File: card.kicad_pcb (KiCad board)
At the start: 2 copper layers, 38.6 x 52.3 mm, 83 parts, among them J1 Conn_01x20_Male, J2 HDMI_A, J3 Conn_01x20_Male, J4 USB_B_Micro, SW1 SW_DPST_x2, U1 SPX3819-1.8, U2 IMP811REUS-T, U3 SP6205EM5-L-3-3_TR, U4 MP1469GJ, U5 W25Q32JVSS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

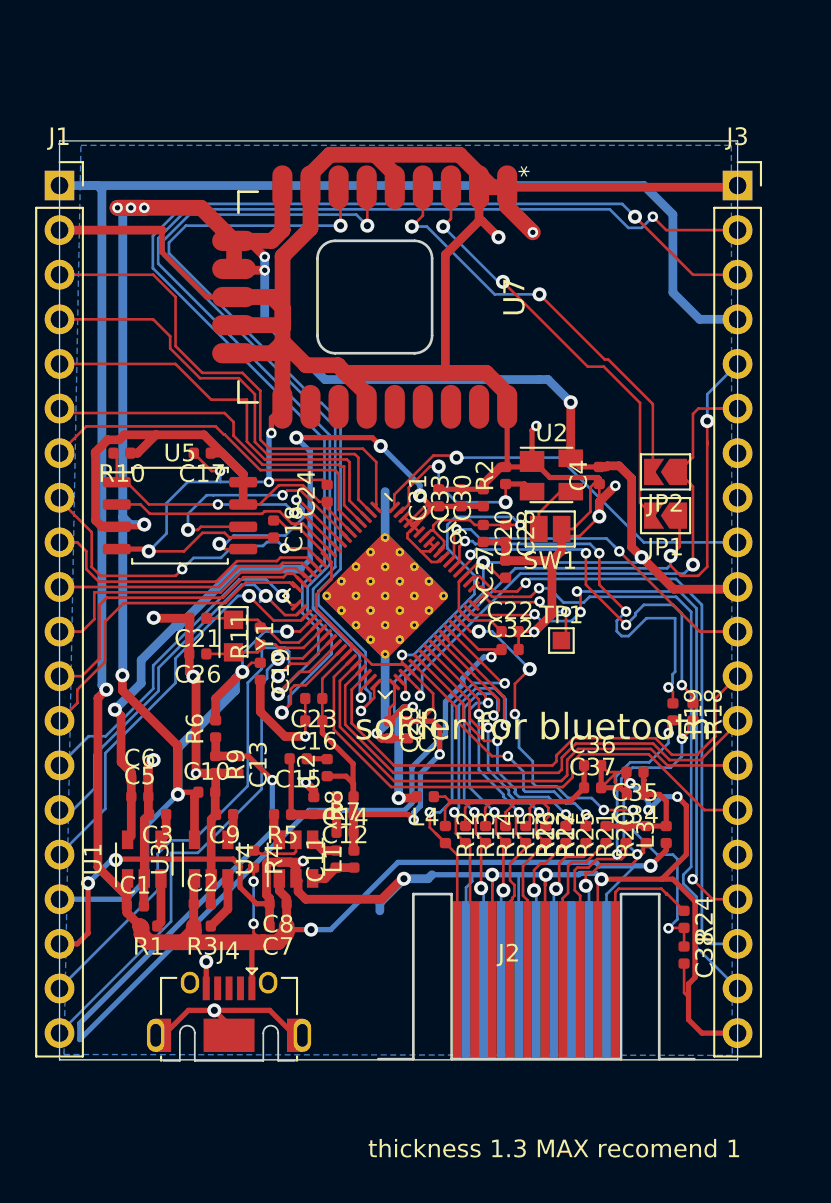
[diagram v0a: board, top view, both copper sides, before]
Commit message: finished routing, and started neatnening up some of the ugly traces and silk screen
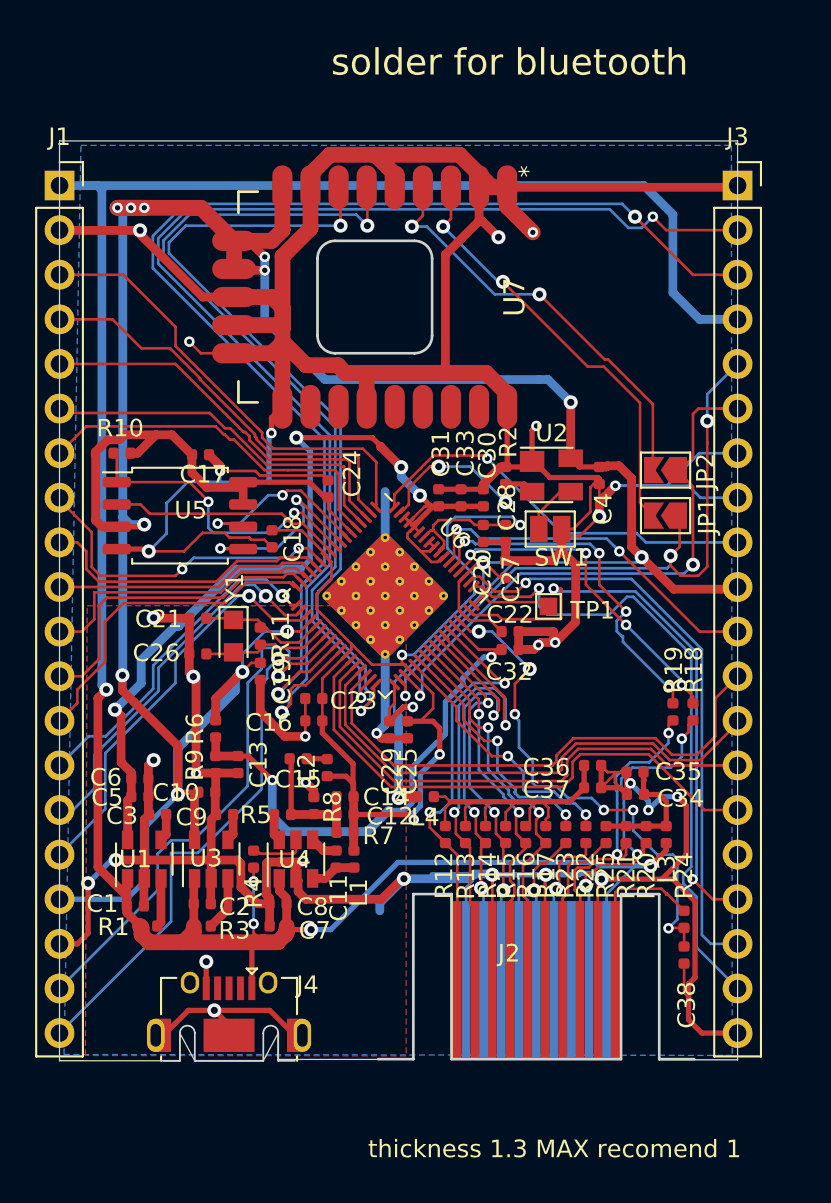
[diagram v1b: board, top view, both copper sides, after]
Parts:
- moved TP1 2.08 mm to (261.8, 83.1)
- moved C18 0.57 mm to (246.0, 79.3)
- moved C24 0.26 mm to (249.2, 76.5)
- moved C17 0.14 mm to (242.0, 74.5), turned to 0 degrees
- moved JP2 0.10 mm to (268.4, 75.4)
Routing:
- net GND: track 344.2 -> 379.2 mm, vias 29 -> 31
- net +2V5: track 63.2 -> 30.4 mm
- net /CPU/SPI_CLK: track 14.8 -> 10.8 mm
- net HDMI_SCL: track 23.9 -> 20.4 mm
- net HDMI_SDA: track 22.4 -> 19.1 mm
- net Net-(TP1-Pad1): track 7.61 -> 4.71 mm, vias 2 -> 0
- net PORT0: track 28.1 -> 25.6 mm
- net /CPU/SPI_CSN: track 15.8 -> 18.2 mm
- net PORT1: track 25.4 -> 23.6 mm
- net AOR: track 35.4 -> 33.9 mm
- net PORT2: track 23.5 -> 22.2 mm
- net UART1-Rx: track 73.1 -> 72.0 mm
- net +3V3: track 206.9 -> 207.8 mm
- net NRST_GX_CPU: track 12.2 -> 11.6 mm
- net VOUT1: track 33.6 -> 33.1 mm, vias 4 -> 2
- added copper zone on F.Cu, net GND
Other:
- board size 38.6 x 52.3 mm -> 38.6 x 52.4 mm
